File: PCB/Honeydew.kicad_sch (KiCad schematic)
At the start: 1 part

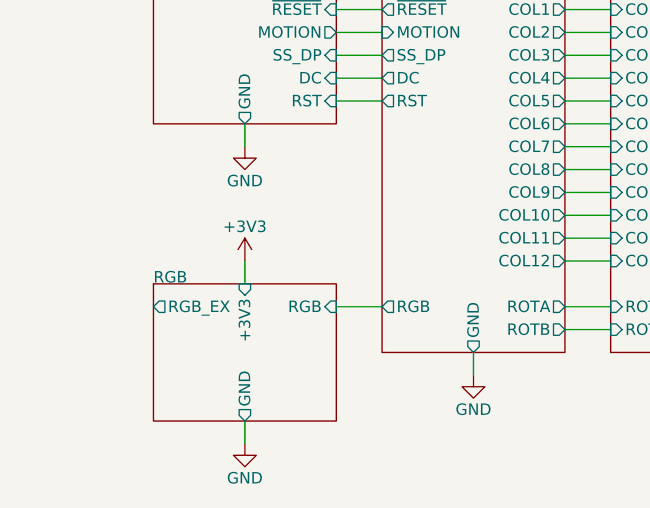
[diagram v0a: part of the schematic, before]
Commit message: Changed RGB LED voltage to 5V.
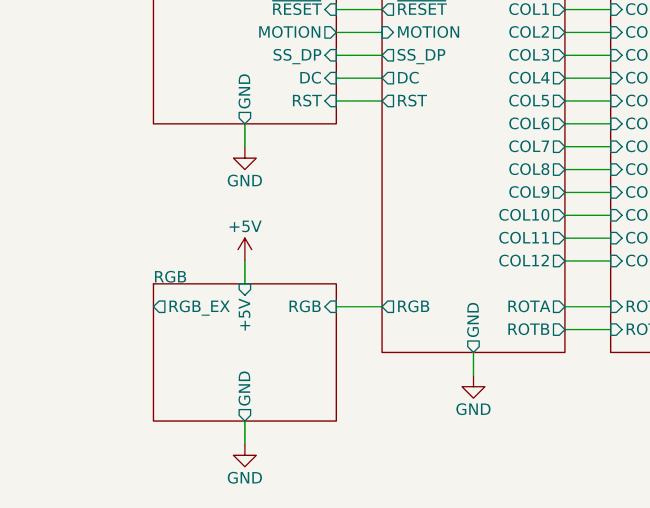
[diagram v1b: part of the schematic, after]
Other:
- sheet RGB ports: added +5V; removed +3V3
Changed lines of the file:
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@@
+    (stroke (width 0) (type default))
+  )
+  (wire (pts (xy 83.82 49.53) (xy 88.9 49.53))
+    (stroke (width 0) (type default))
+  )
+  (wire (pts (xy 99.06 21.59) (xy 99.06 24.13))
+    (stroke (width 0) (type default))
+  )
+  (wire (pts (xy 83.82 59.69) (xy 88.9 59.69))
+    (stroke (width 0) (type default))
+  )
+  (wire (pts (xy 58.42 54.61) (xy 63.5 54.61))
+    (stroke (width 0) (type default))
+  )
+  (wire (pts (xy 83.82 64.77) (xy 88.9 64.77))
+    (stroke (width 0) (type default))
+  )
+  (wire (pts (xy 58.42 46.99) (xy 63.5 46.99))
+    (stroke (width 0) (type default))
+  )
+  (wire (pts (xy 83.82 62.23) (xy 88.9 62.23))
+    (stroke (width 0) (type default))
+  )
+  (wire (pts (xy 58.42 39.37) (xy 63.5 39.37))
+    (stroke (width 0) (type default))
+  )
+  (wire (pts (xy 83.82 34.29) (xy 88.9 34.29))
+    (stroke (width 0) (type default))
+  )
+  (wire (pts (xy 38.1 31.75) (xy 30.48 31.75))
+    (stroke (width 0) (type default))
+  )
+  (wire (pts (xy 30.48 31.75) (xy 30.48 26.67))
     (stroke (width 0) (type default))
   )
   (wire (pts (xy 48.26 72.39) (xy 48.26 74.93))
-    (stroke (width 0) (type default))
-  )
-  (wire (pts (xy 83.82 49.53) (xy 88.9 49.53))
-    (stroke (width 0) (type default))
-  )
-  (wire (pts (xy 99.06 21.59) (xy 99.06 24.13))
-    (stroke (width 0) (type default))
-  )
-  (wire (pts (xy 83.82 59.69) (xy 88.9 59.69))
-    (stroke (width 0) (type default))
-  )
-  (wire (pts (xy 58.42 54.61) (xy 63.5 54.61))
-    (stroke (width 0) (type default))
-  )
-  (wire (pts (xy 83.82 64.77) (xy 88.9 64.77))
-    (stroke (width 0) (type default))
-  )
-  (wire (pts (xy 58.42 46.99) (xy 63.5 46.99))
-    (stroke (width 0) (type default))
-  )
-  (wire (pts (xy 83.82 62.23) (xy 88.9 62.23))
-    (stroke (width 0) (type default))
-  )
-  (wire (pts (xy 58.42 39.37) (xy 63.5 39.37))
-    (stroke (width 0) (type default))
-  )
-  (wire (pts (xy 83.82 34.29) (xy 88.9 34.29))
-    (stroke (width 0) (type default))
-  )
-  (wire (pts (xy 38.1 31.75) (xy 30.48 31.75))
-    (stroke (width 0) (type default))
-  )
-  (wire (pts (xy 30.48 31.75) (xy 30.48 26.67))
     (stroke (width 0) (type default))
   )
@@
     )
   )
-  (symbol (lib_id "power:+3V3") (at 48.26 72.39 0) (unit 1)
-    (in_bom yes) (on_board yes) (dnp no)
-    (property "Reference" "#PWR0107" (at 48.26 76.2 0)
-      (effects (font (size 1.27 1.27)) hide)
-    )
-    (property "Value" "+3V3" (at 48.26 68.58 0)
+  (symbol (lib_id "power:GND") (at 73.66 85.09 0) (unit 1)
+    (in_bom yes) (on_board yes) (dnp no)
+    (property "Reference" "#PWR07" (at 73.66 91.44 0)
+      (effects (font (size 1.27 1.27)) hide)
+    )
+    (property "Value" "GND" (at 73.66 88.9 0)
+      (effects (font (size 1.27 1.27)))
+    )
+    (property "Footprint" "" (at 73.66 85.09 0)
+      (effects (font (size 1.27 1.27)) hide)
+    )
+    (property "Datasheet" "" (at 73.66 85.09 0)
+      (effects (font (size 1.27 1.27)) hide)
+    )
+    (pin "1")
+    (instances
+      (project "Honeydew"
+        (path "/534caec7-cf60-4f90-b1ed-42c9d445ef0f"
+          (reference "#PWR07") (unit 1)
+        )
+      )
+    )
+  )
+  (symbol (lib_id "power:+5V") (at 48.26 72.39 0) (mirror y) (unit 1)
+    (in_bom yes) (on_board yes) (dnp no)
+    (property "Reference" "#PWR02" (at 48.26 76.2 0)
+      (effects (font (size 1.27 1.27)) hide)
+    )
+    (property "Value" "+5V" (at 48.26 68.58 0)
       (effects (font (size 1.27 1.27)))
     )
@@
       (project "Honeydew"
         (path "/534caec7-cf60-4f90-b1ed-42c9d445ef0f"
-          (reference "#PWR0107") (unit 1)
-        )
-      )
-    )
-  )
-  (symbol (lib_id "power:GND") (at 73.66 85.09 0) (unit 1)
-    (in_bom yes) (on_board yes) (dnp no)
-    (property "Reference" "#PWR07" (at 73.66 91.44 0)
-      (effects (font (size 1.27 1.27)) hide)
-    )
-    (property "Value" "GND" (at 73.66 88.9 0)
-      (effects (font (size 1.27 1.27)))
-    )
-    (property "Footprint" "" (at 73.66 85.09 0)
-      (effects (font (size 1.27 1.27)) hide)
-    )
-    (property "Datasheet" "" (at 73.66 85.09 0)
-      (effects (font (size 1.27 1.27)) hide)
-    )
-    (pin "1")
-    (instances
-      (project "Honeydew"
-        (path "/534caec7-cf60-4f90-b1ed-42c9d445ef0f"
-          (reference "#PWR07") (unit 1)
+          (reference "#PWR02") (unit 1)
         )
       )
@@
       (effects (font (size 1.27 1.27)) (justify right))
     )
-    (pin "+3V3" input (at 48.26 74.93 90)
-      (effects (font (size 1.27 1.27)) (justify right))
-    )
     (pin "RGB_EX" output (at 38.1 77.47 180)
       (effects (font (size 1.27 1.27)) (justify left))
     )
-    (instances
+    (pin "+5V" input (at 48.26 74.93 90)
+      (effects (font (size 1.27 1.27)) (justify right))
+    )
+    (instances

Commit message: Massive mistake corrections and clarifications.
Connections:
- no-connect marks 0 -> 1
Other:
- sheet Comms ports: added none; removed +2V, +3V3, +5V, GND, VBUS
- sheet MCU ports: added none; removed +3V3, GND
- sheet Matrix ports: added none; removed +3V3, GND
- sheet PSU ports: added none; removed +2V, +3V3, +5V, GND
- sheet RGB ports: added none; removed +5V, GND

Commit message: Shifted MCU up to reduce length of USB traces. Added holes for JLC assembly.
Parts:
- added H1, H2, H3: Tooling Hole, Honeydew:JLC Tooling Hole, symbol Mechanical:MountingHole
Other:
- moved on the sheet: A1
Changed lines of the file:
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@@
     (stroke (width 0) (type default))
   )
-  (symbol (lib_id "Mechanical:MountingHole") (at 137.16 45.72 0) (unit 1)
+  (symbol (lib_id "Mechanical:MountingHole") (at 116.84 39.37 0) (unit 1)
     (in_bom no) (on_board yes) (dnp no)
-    (property "Reference" "A1" (at 139.7 44.5516 0)
+    (property "Reference" "A1" (at 119.38 38.2016 0)
       (effects (font (size 1.27 1.27)) (justify left))
     )
-    (property "Value" "Art" (at 139.7 46.863 0)
+    (property "Value" "Art" (at 119.38 40.513 0)
       (effects (font (size 1.27 1.27)) (justify left))
     )
-    (property "Footprint" "Honeydew:Ariamelon_Logo_x3_CU" (at 137.16 45.72 0)
+    (property "Footprint" "Honeydew:Ariamelon_Logo_x3_CU" (at 116.84 39.37 0)
       (effects (font (size 1.27 1.27)) hide)
     )
-    (property "Datasheet" "~" (at 137.16 45.72 0)
+    (property "Datasheet" "~" (at 116.84 39.37 0)
       (effects (font (size 1.27 1.27)) hide)
     )
-    (property "LCSC" "" (at 137.16 45.72 0)
+    (property "LCSC" "" (at 116.84 39.37 0)
       (effects (font (size 1.27 1.27)) hide)
     )
@@
         )
       )
+    )
+  )
+  (symbol (lib_id "Mechanical:MountingHole") (at 116.84 62.23 0) (unit 1)
+    (in_bom no) (on_board yes) (dnp no)
+    (property "Reference" "H3" (at 119.38 61.0616 0)
+      (effects (font (size 1.27 1.27)) (justify left))
+    )
+    (property "Value" "Tooling Hole" (at 119.38 63.373 0)
+      (effects (font (size 1.27 1.27)) (justify left))
+    )
+    (property "Footprint" "Honeydew:JLC Tooling Hole" (at 116.84 62.23 0)
+      (effects (font (size 1.27 1.27)) hide)
+    )
+    (property "Datasheet" "~" (at 116.84 62.23 0)
+      (effects (font (size 1.27 1.27)) hide)
+    )
+    (property "LCSC" "" (at 116.84 62.23 0)
+      (effects (font (size 1.27 1.27)) hide)
+    )
+    (instances
+      (project "Honeydew"
+        (path "/534caec7-cf60-4f90-b1ed-42c9d445ef0f"
+          (reference "H3") (unit 1)
+        )
+      )
+    )
+  )
+  (symbol (lib_id "Mechanical:MountingHole") (at 116.84 52.07 0) (unit 1)
+    (in_bom no) (on_board yes) (dnp no)
+    (property "Reference" "H1" (at 119.38 50.9016 0)
+      (effects (font (size 1.27 1.27)) (justify left))
+    )
+    (property "Value" "Tooling Hole" (at 119.38 53.213 0)
+      (effects (font (size 1.27 1.27)) (justify left))
+    )
+    (property "Footprint" "Honeydew:JLC Tooling Hole" (at 116.84 52.07 0)
+      (effects (font (size 1.27 1.27)) hide)
+    )
+    (property "Datasheet" "~" (at 116.84 52.07 0)
+      (effects (font (size 1.27 1.27)) hide)
+    )
+    (property "LCSC" "" (at 116.84 52.07 0)
+      (effects (font (size 1.27 1.27)) hide)
+    )
+    (instances
+      (project "Honeydew"
+        (path "/534caec7-cf60-4f90-b1ed-42c9d445ef0f"
+          (reference "H1") (unit 1)
+        )
+      )
+    )
+  )
+  (symbol (lib_id "Mechanical:MountingHole") (at 116.84 57.15 0) (unit 1)
+    (in_bom no) (on_board yes) (dnp no)
+    (property "Reference" "H2" (at 119.38 55.9816 0)
+      (effects (font (size 1.27 1.27)) (justify left))
+    )
+    (property "Value" "Tooling Hole" (at 119.38 58.293 0)
+      (effects (font (size 1.27 1.27)) (justify left))
+    )
+    (property "Footprint" "Honeydew:JLC Tooling Hole" (at 116.84 57.15 0)
+      (effects (font (size 1.27 1.27)) hide)
+    )
+    (property "Datasheet" "~" (at 116.84 57.15 0)
+      (effects (font (size 1.27 1.27)) hide)
+    )
+    (property "LCSC" "" (at 116.84 57.15 0)
+      (effects (font (size 1.27 1.27)) hide)
+    )
+    (instances
+      (project "Honeydew"
+        (path "/534caec7-cf60-4f90-b1ed-42c9d445ef0f"
+          (reference "H2") (unit 1)
+        )
+      )

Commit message: Added level shifter to the RGB signal, just in case.
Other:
- sheet Comms ports: added RST_OLED, SS_OLED, SS_TB, ~{RST}_TB; removed RST, SS_DP, SS_TP, ~{RESET}
- sheet MCU ports: added RST_OLED, SS_OLED, SS_TB, ~{RST}_TB; removed RST, SS_DP, SS_TP, ~{RESET}
- title: Honeydew unsplit ergonomic keyboard -> Honeydew unified split ergonomic keyboard
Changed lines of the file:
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@@
   (paper "A5")
   (title_block
-    (title "Honeydew unsplit ergonomic keyboard")
-    (date "2022-05-30")
-    (rev "V2.1")
+    (title "Honeydew unified split ergonomic keyboard")
+    (date "2023-03-18")
+    (rev "V1.1")
   )
   (no_connect (at 38.1 77.47))
@@
       (effects (font (size 1.27 1.27)) (justify right))
     )
-    (pin "SS_TP" input (at 58.42 41.91 0)
-      (effects (font (size 1.27 1.27)) (justify right))
-    )
     (pin "MISO" output (at 58.42 36.83 0)
       (effects (font (size 1.27 1.27)) (justify right))
     )
-    (pin "~{RESET}" input (at 58.42 44.45 0)
-      (effects (font (size 1.27 1.27)) (justify right))
-    )
     (pin "MOTION" output (at 58.42 46.99 0)
       (effects (font (size 1.27 1.27)) (justify right))
@@
       (effects (font (size 1.27 1.27)) (justify right))
     )
-    (pin "RST" input (at 58.42 54.61 0)
-      (effects (font (size 1.27 1.27)) (justify right))
-    )
-    (pin "SS_DP" input (at 58.42 49.53 0)
+    (pin "RST_OLED" input (at 58.42 54.61 0)
+      (effects (font (size 1.27 1.27)) (justify right))
+    )
+    (pin "~{RST}_TB" input (at 58.42 44.45 0)
+      (effects (font (size 1.27 1.27)) (justify right))
+    )
+    (pin "SS_OLED" input (at 58.42 49.53 0)
+      (effects (font (size 1.27 1.27)) (justify right))
+    )
+    (pin "SS_TB" input (at 58.42 41.91 0)
       (effects (font (size 1.27 1.27)) (justify right))
     )
@@
       (effects (font (size 1.27 1.27)) (justify left))
     )
-    (pin "SS_TP" output (at 63.5 41.91 180)
-      (effects (font (size 1.27 1.27)) (justify left))
-    )
     (pin "MOTION" input (at 63.5 46.99 180)
       (effects (font (size 1.27 1.27)) (justify left))
     )
-    (pin "~{RESET}" output (at 63.5 44.45 180)
-      (effects (font (size 1.27 1.27)) (justify left))
-    )
     (pin "COL12" output (at 83.82 72.39 0)
       (effects (font (size 1.27 1.27)) (justify right))
@@
       (effects (font (size 1.27 1.27)) (justify left))
     )
-    (pin "SS_DP" output (at 63.5 49.53 180)
-      (effects (font (size 1.27 1.27)) (justify left))
-    )
     (pin "DC" output (at 63.5 52.07 180)
       (effects (font (size 1.27 1.27)) (justify left))
     )
-    (pin "RST" output (at 63.5 54.61 180)
-      (effects (font (size 1.27 1.27)) (justify left))
-    )
+    (pin "SS_OLED" output (at 63.5 49.53 180)
+      (effects (font (size 1.27 1.27)) (justify left))
+    )
+    (pin "RST_OLED" output (at 63.5 54.61 180)
+      (effects (font (size 1.27 1.27)) (justify left))
+    )
+    (pin "~{RST}_TB" output (at 63.5 44.45 180)
+      (effects (font (size 1.27 1.27)) (justify left))
+    )
+    (pin "SS_TB" output (at 63.5 41.91 180)
+      (effects (font (size 1.27 1.27)) (justify left))
+    )

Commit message: More V1.1 updates
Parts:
- added A2: Art, Honeydew:QMK Logo, symbol Mechanical:Fiducial
- A1: symbol Mechanical:MountingHole -> Mechanical:Fiducial; now in the parts list
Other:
- sheet Comms ports: added DC_OLED, ~{RST}; removed DC, RST_OLED, ~{RST}_TB
- sheet MCU ports: added DC_OLED, ROTC, ~{RST}; removed DC, RST_OLED, ~{RST}_TB
- sheet Matrix ports: added ROTC; removed none
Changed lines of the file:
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@@
   (title_block
     (title "Honeydew unified split ergonomic keyboard")
-    (date "2023-03-18")
+    (date "2023-03-31")
     (rev "V1.1")
   )
@@
     (stroke (width 0) (type default))
   )
-  (wire (pts (xy 58.42 54.61) (xy 63.5 54.61))
-    (stroke (width 0) (type default))
-  )
   (wire (pts (xy 83.82 64.77) (xy 88.9 64.77))
     (stroke (width 0) (type default))
@@
     (stroke (width 0) (type default))
   )
+  (wire (pts (xy 83.82 82.55) (xy 88.9 82.55))
+    (stroke (width 0) (type default))
+  )
   (wire (pts (xy 83.82 54.61) (xy 88.9 54.61))
     (stroke (width 0) (type default))
@@
     (stroke (width 0) (type default))
   )
-  (symbol (lib_id "Mechanical:MountingHole") (at 116.84 39.37 0) (unit 1)
-    (in_bom no) (on_board yes) (dnp no)
+  (symbol (lib_id "Mechanical:Fiducial") (at 116.84 39.37 0) (unit 1)
+    (in_bom yes) (on_board yes) (dnp no)
     (property "Reference" "A1" (at 119.38 38.2016 0)
       (effects (font (size 1.27 1.27)) (justify left))
@@
         (path "/534caec7-cf60-4f90-b1ed-42c9d445ef0f"
           (reference "H3") (unit 1)
+        )
+      )
+    )
+  )
+  (symbol (lib_id "Mechanical:Fiducial") (at 116.84 44.45 0) (unit 1)
+    (in_bom yes) (on_board yes) (dnp no)
+    (property "Reference" "A2" (at 119.38 43.2816 0)
+      (effects (font (size 1.27 1.27)) (justify left))
+    )
+    (property "Value" "Art" (at 119.38 45.593 0)
+      (effects (font (size 1.27 1.27)) (justify left))
+    )
+    (property "Footprint" "Honeydew:QMK Logo" (at 116.84 44.45 0)
+      (effects (font (size 1.27 1.27)) hide)
+    )
+    (property "Datasheet" "~" (at 116.84 44.45 0)
+      (effects (font (size 1.27 1.27)) hide)
+    )
+    (property "LCSC" "" (at 116.84 44.45 0)
+      (effects (font (size 1.27 1.27)) hide)
+    )
+    (instances
+      (project "Honeydew"
+        (path "/534caec7-cf60-4f90-b1ed-42c9d445ef0f"
+          (reference "A2") (unit 1)
         )
       )
@@
     )
   )
-  (sheet (at 38.1 24.13) (size 20.32 33.02)
+  (sheet (at 38.1 24.13) (size 20.32 30.48)
     (stroke (width 0.1524) (type solid))
     (fill (color 0 0 0 0.0000))
@@
       (effects (font (size 1.27 1.27)) (justify right))
     )
-    (pin "DC" input (at 58.42 52.07 0)
-      (effects (font (size 1.27 1.27)) (justify right))
-    )
-    (pin "RST_OLED" input (at 58.42 54.61 0)
-      (effects (font (size 1.27 1.27)) (justify right))
-    )
-    (pin "~{RST}_TB" input (at 58.42 44.45 0)
-      (effects (font (size 1.27 1.27)) (justify right))
-    )
     (pin "SS_OLED" input (at 58.42 49.53 0)
       (effects (font (size 1.27 1.27)) (justify right))
     )
     (pin "SS_TB" input (at 58.42 41.91 0)
+      (effects (font (size 1.27 1.27)) (justify right))
+    )
+    (pin "DC_OLED" input (at 58.42 52.07 0)
+      (effects (font (size 1.27 1.27)) (justify right))
+    )
+    (pin "~{RST}" input (at 58.42 44.45 0)
       (effects (font (size 1.27 1.27)) (justify right))
     )
@@
     )
   )
-  (sheet (at 88.9 24.13) (size 20.32 58.42)
+  (sheet (at 88.9 24.13) (size 20.32 60.96)
     (stroke (width 0.1524) (type solid))
     (fill (color 0 0 0 0.0000))
@@
       (effects (font (size 1.27 1.27)) (justify left))
     )
+    (pin "ROTC" input (at 88.9 82.55 180)
+      (effects (font (size 1.27 1.27)) (justify left))
+    )
     (instances
       (project "Honeydew"
@@
     )
   )
-  (sheet (at 63.5 24.13) (size 20.32 58.42)
+  (sheet (at 63.5 24.13) (size 20.32 60.96)
     (stroke (width 0.1524) (type solid))
     (fill (color 0 0 0 0.0000))
@@
       (effects (font (size 1.27 1.27)) (justify left))
     )
-    (pin "DC" output (at 63.5 52.07 180)
-      (effects (font (size 1.27 1.27)) (justify left))
-    )
     (pin "SS_OLED" output (at 63.5 49.53 180)
       (effects (font (size 1.27 1.27)) (justify left))
     )
-    (pin "RST_OLED" output (at 63.5 54.61 180)
-      (effects (font (size 1.27 1.27)) (justify left))
-    )
-    (pin "~{RST}_TB" output (at 63.5 44.45 180)
-      (effects (font (size 1.27 1.27)) (justify left))
-    )
     (pin "SS_TB" output (at 63.5 41.91 180)
       (effects (font (size 1.27 1.27)) (justify left))
     )
-    (instances
+    (pin "DC_OLED" output (at 63.5 52.07 180)
+      (effects (font (size 1.27 1.27)) (justify left))
+    )
+    (pin "~{RST}" output (at 63.5 44.45 180)
+      (effects (font (size 1.27 1.27)) (justify left))
+    )
+    (pin "ROTC" output (at 83.82 82.55 0)
+      (effects (font (size 1.27 1.27)) (justify right))
+    )
+    (instances

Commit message: Initial V2.0 update.
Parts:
- added J9: RGB_EX, Honeydew:PinHeader_1x04_P2.54mm_Vertical_SIlkless, symbol Connector_Generic:Conn_01x04
- A1: value Art -> Ariamelon Logo
- A2: value Art -> QMK Logo
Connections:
- net RGB/RGB_EX: now also J9.1 (Pin_1)
- new net +5V: J9.2 (Pin_2)
- new net GND: J9.3 (Pin_3), J9.4 (Pin_4)
- no-connect marks 1 -> 0
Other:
- sheet Comms renamed USB
- added sheet Expansion (Expansion.kicad_sch)
- sheet MCU ports: added RX, TX; removed none
- sheet USB: file Comms.kicad_sch -> USB.kicad_sch
- sheet USB ports: added none; removed DC_OLED, MISO, MOSI, MOTION, SCK, SS_OLED, SS_TB, ~{RST}
